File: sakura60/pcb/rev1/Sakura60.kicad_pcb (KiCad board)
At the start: 2 copper layers, 268 x 106.7 mm, 327 parts, among them J1 OLED, J2 Conn_1x02, SW1 SW_PUSH, SW10 SW_PUSH, SW11 SW_PUSH, SW12 SW_PUSH, SW13 SW_PUSH, SW14 SW_PUSH, SW15 SW_PUSH, SW16 SW_PUSH, SW17 SW_PUSH, SW18 SW_PUSH, SW19 SW_PUSH, SW2 SW_PUSH, SW20 SW_PUSH, SW21 SW_PUSH, SW22 SW_PUSH, SW23 SW_PUSH, SW24 SW_PUSH, SW25 SW_PUSH, SW26 SW_PUSH, SW27 SW_PUSH, SW28 SW_PUSH, SW29 SW_PUSH, SW3 SW_PUSH, SW30 SW_PUSH, SW31 SW_PUSH, SW32 SW_PUSH, SW33 SW_PUSH, SW34 SW_PUSH, SW35 SW_PUSH, SW36 SW_PUSH, SW37 SW_PUSH, SW38 SW_PUSH, SW39 SW_PUSH, SW4 SW_PUSH, SW40 SW_PUSH, SW41 SW_PUSH, SW42 SW_PUSH, SW43 SW_PUSH, SW44 SW_PUSH, SW45 SW_PUSH, SW46 SW_PUSH, SW47 SW_PUSH, SW48 SW_PUSH, SW49 SW_PUSH, SW5 SW_PUSH, SW50 SW_PUSH, SW51 SW_PUSH, SW52 SW_PUSH, SW53 SW_PUSH, SW54 SW_PUSH, SW55 SW_PUSH, SW56 SW_PUSH, SW57 SW_PUSH, SW58 SW_PUSH, SW59 SW_PUSH, SW6 SW_PUSH, SW61 Rotary_Encoder_Switch, SW7 SW_PUSH, SW8 SW_PUSH, SW9 SW_PUSH, U1 BlueMacro

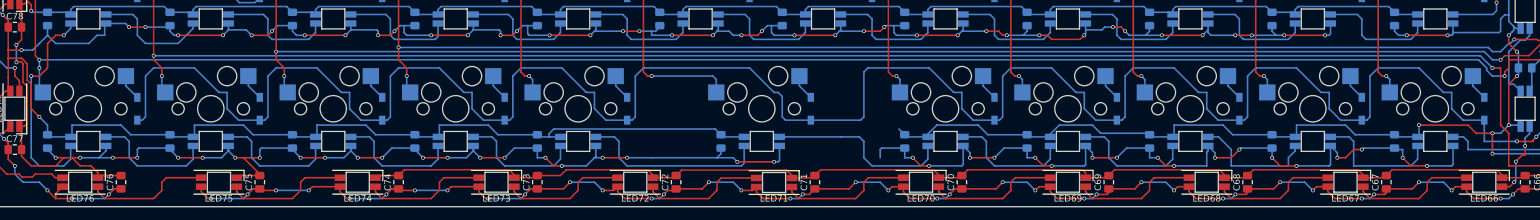
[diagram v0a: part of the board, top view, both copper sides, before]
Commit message: Added stablizer for 2U spacebar
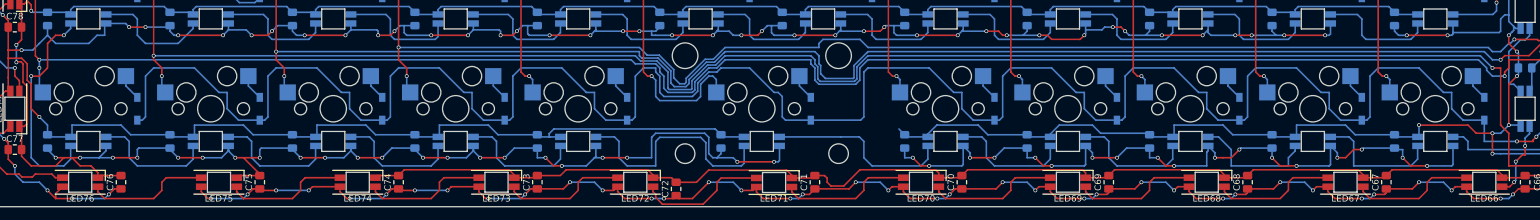
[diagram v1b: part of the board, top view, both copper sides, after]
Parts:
- added REF**: 2U, MX_Only:MXOnly-2U-ReversedStabilizers-NoSwitch, F.Cu at (140.3, 111.8)
- moved C72 1.05 mm to (127.0, 124.2)
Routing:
- net col1: track 416.1 -> 428.6 mm
- net col2: track 341.2 -> 353.6 mm
- net col0: track 425.3 -> 437.5 mm
- net Net-(LED6-Pad2): track 29.3 -> 36.7 mm
- net col3: track 328.1 -> 335.3 mm
- net row4: track 427.6 -> 433.9 mm
- net col5: track 298.6 -> 304.4 mm
- net GND: track 2222.8 -> 2226.6 mm
- net Net-(LED71-Pad2): track 19.4 -> 20.4 mm

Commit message: Add some project
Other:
- net class Default removed
